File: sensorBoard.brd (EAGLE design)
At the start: 20 x 50 mm, 35 parts, among them Q1 BSS84, U1 ADXL345, U2 L3G4200D, U3 MPL115A, X1 22-23-2051

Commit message: Tweaked silkscreen Removed some overlaps Moved Logo
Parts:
- moved U$10 14.6 mm to (9.70, 18.1), turned to 90 degrees
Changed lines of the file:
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@@
 <attribute name="VALUE" x="18.005" y="35.765" size="0.8" layer="27" rot="R90"/>
 </element>
-<element name="U$10" library="earsLogo" package="EARS-LOGO" value="EARS-LOGO" x="9.4" y="32.7" rot="MR0"/>
+<element name="U$10" library="earsLogo" package="EARS-LOGO" value="EARS-LOGO" x="9.7" y="18.1" rot="MR90"/>
 </elements>
 <signals>

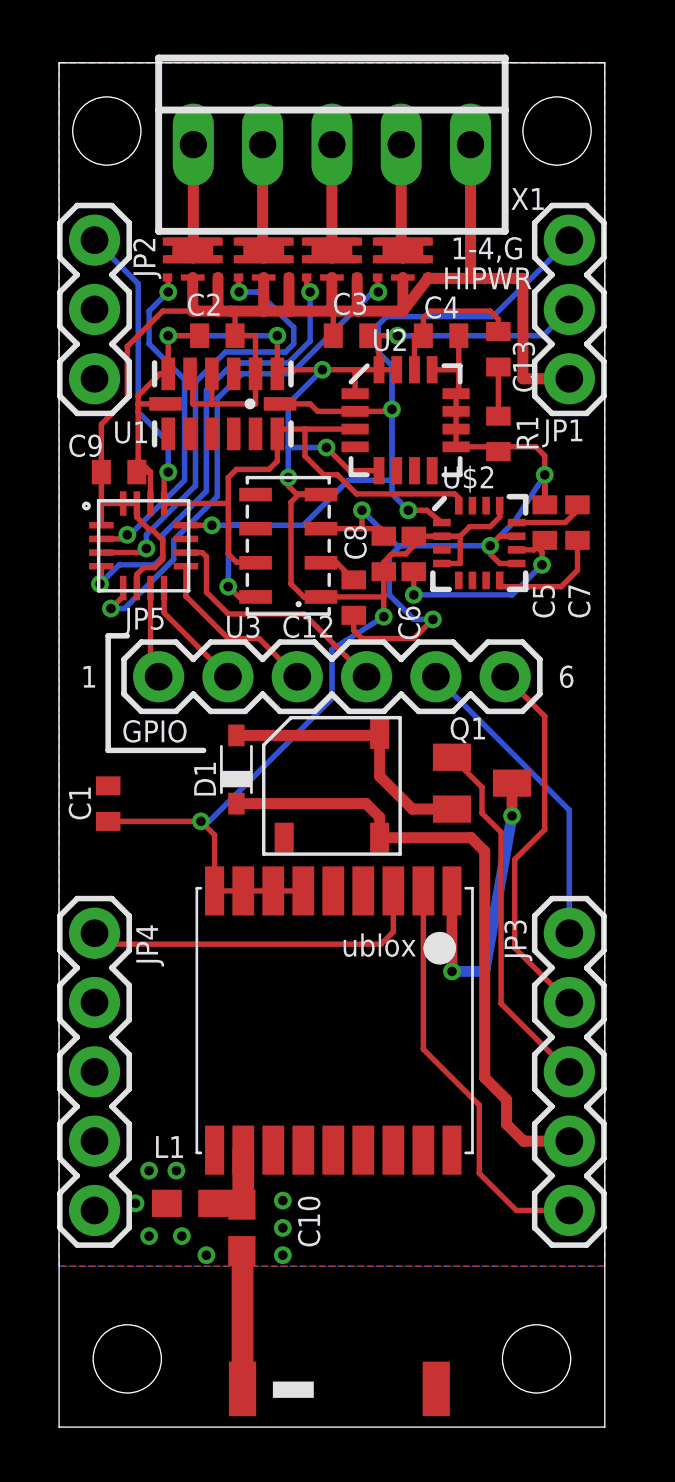
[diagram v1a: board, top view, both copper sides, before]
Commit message: Added pull-up resistors on mosfets
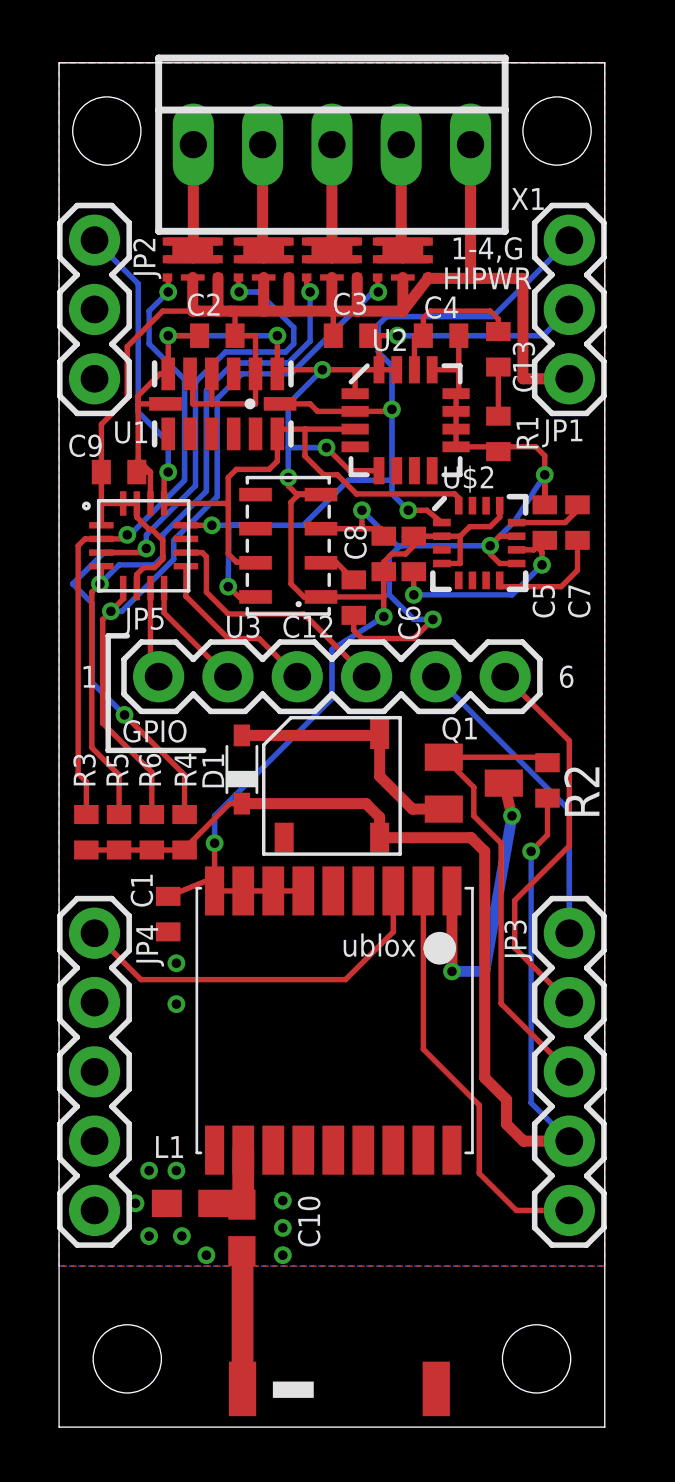
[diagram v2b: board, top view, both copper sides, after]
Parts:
- added R2, R3, R4, R5, R6: 10k, rcl:R0402
- moved C1 4.61 mm to (4.00, 18.8), turned to 270 degrees
- moved Q1 0.30 mm to (15.2, 23.6)
- moved D1 0.20 mm to (6.70, 24.1)
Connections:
- net GPIO3: now also R2.1
- net P0: now also R3.1
- net P1: now also R4.1
- net P2: now also R5.1
- net P3: now also R6.1
- net VBAT: now also R2.2, R3.2, R4.2, R5.2, R6.2
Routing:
- net VBAT: track 23.2 -> 42.8 mm, vias 0 -> 1
- net P1: track 16.4 -> 29.8 mm, vias 2 -> 3
- net P0: track 12.2 -> 23.1 mm
- net P2: track 17.1 -> 26.1 mm
- net P3: track 18.6 -> 27.1 mm
- net GPIO3: track 13.3 -> 17.4 mm
- net VCC: track 76.7 -> 74.6 mm
- net GPS_RX: track 12.8 -> 13.9 mm
- net GPIO2: track 13.8 -> 14.6 mm
- net N$5: track 10.00 -> 9.50 mm
- net GND: vias 15 -> 17

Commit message: Final silk check, added labels and license, shifted rf trace ground plane last time xD
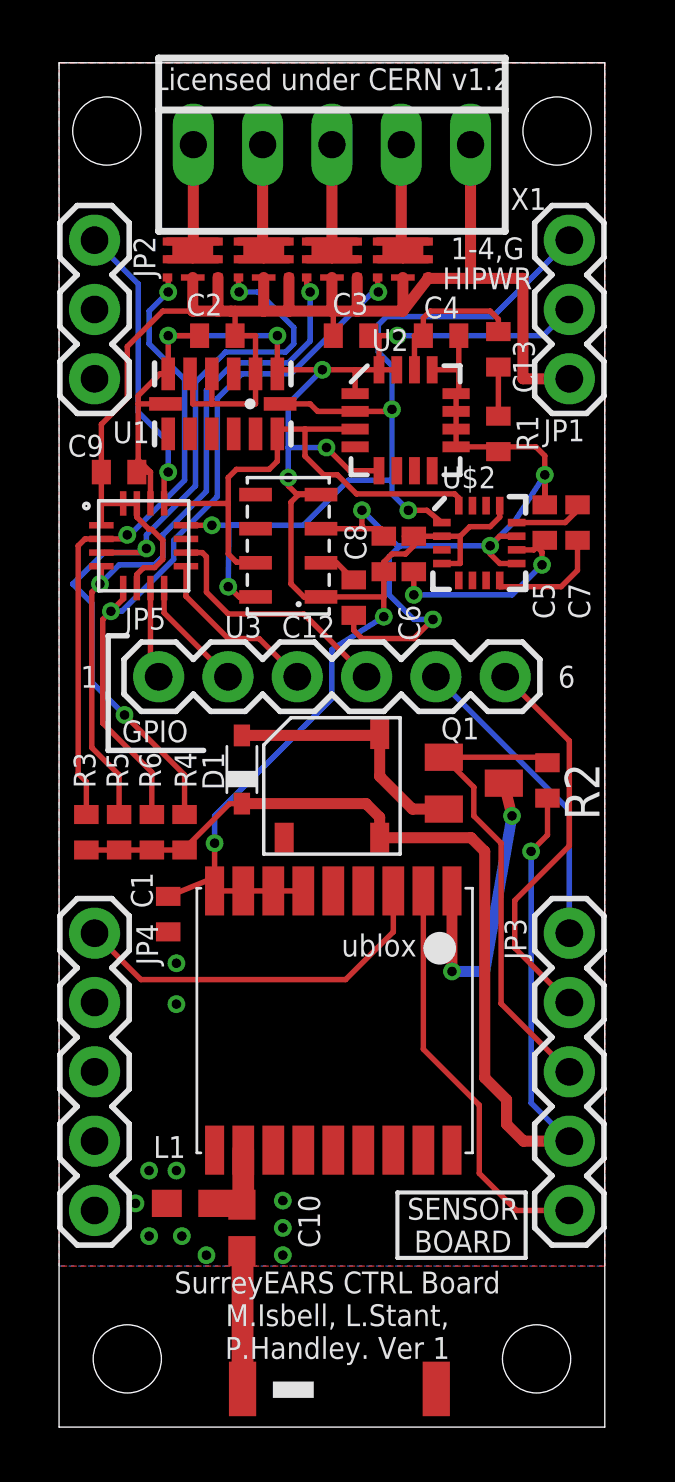
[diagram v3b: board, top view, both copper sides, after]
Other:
- board text added: "Licensed under CERN v1.2"
- board text added: "SENSOR BOARD"
- board text added: "SurreyEARS CTRL Board M.Isbell, L.Stant, P.Handley. Ver 1"
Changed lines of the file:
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@@
 <rectangle x1="15" y1="0" x2="20" y2="5" layer="39"/>
 <polygon width="0" layer="41">
-<vertex x="5.9" y="9.2"/>
-<vertex x="7.6" y="9.2"/>
-<vertex x="7.6" y="5.7"/>
-<vertex x="5.9" y="5.7"/>
+<vertex x="6" y="9.2"/>
+<vertex x="7.4" y="9.2"/>
+<vertex x="7.4" y="5.7"/>
+<vertex x="6" y="5.7"/>
 </polygon>
 <polygon width="0" layer="41">
@@
 <text x="15.7" y="42.1" size="0.8" layer="25" font="vector" ratio="20" align="center">HIPWR</text>
 <text x="15.7" y="43.2" size="0.8" layer="25" font="vector" ratio="20" align="center">1-4,G</text>
+<text x="10.2" y="2.5" size="0.8" layer="25" font="vector" ratio="20" align="bottom-center">SurreyEARS CTRL Board
+M.Isbell, L.Stant,
+P.Handley. Ver 1</text>
+<text x="10" y="49" size="0.8" layer="25" font="vector" ratio="20" align="bottom-center">Licensed under CERN v1.2</text>
+<text x="14.8" y="7.4" size="0.8" layer="25" font="vector" ratio="20" align="center">SENSOR
+BOARD</text>
+<wire x1="12.4" y1="8.6" x2="17.1" y2="8.6" width="0.15" layer="25"/>
+<wire x1="17.1" y1="8.6" x2="17.1" y2="6.2" width="0.15" layer="25"/>
+<wire x1="17.1" y1="6.2" x2="12.4" y2="6.2" width="0.15" layer="25"/>
+<wire x1="12.4" y1="6.2" x2="12.4" y2="8.6" width="0.15" layer="25"/>
 </plain>
 <attributes>
@@
 </board>
 </drawing>
+<compatibility>
+<note version="6.3" minversion="6.2.2" severity="warning">
+Since Version 6.2.2 text objects can contain more than one line,
+which will not be processed correctly with this version.
+</note>
+</compatibility>
 </eagle>
